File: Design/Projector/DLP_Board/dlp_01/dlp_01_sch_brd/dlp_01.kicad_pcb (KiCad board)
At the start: 6 copper layers, 102 x 98 mm, 238 parts, among them J1 Conn_02x40_Odd_Even, J2 Conn_02x40_Odd_Even, J3 Barrel_Jack_MountingPin, J4 Screw_Terminal_01x03, J5 Screw_Terminal_01x03, J6 Conn_01x03_Male, J7 Conn_01x03_Male, J8 Conn_01x03_Male, J9 Conn_01x03_Male, Q1 2N7000, U1 DLPC3437, U2 DLPC3437, U3 ASDMB-24.000MHZ-LC-T, U4 W25Q64JVSSIQ, U5 W25Q64JVSSIQ, U6 DLPA3000, U7 DLP3310AFQM, U8 RPM5.0-3.0, U9 NF_SN74AUP1T17

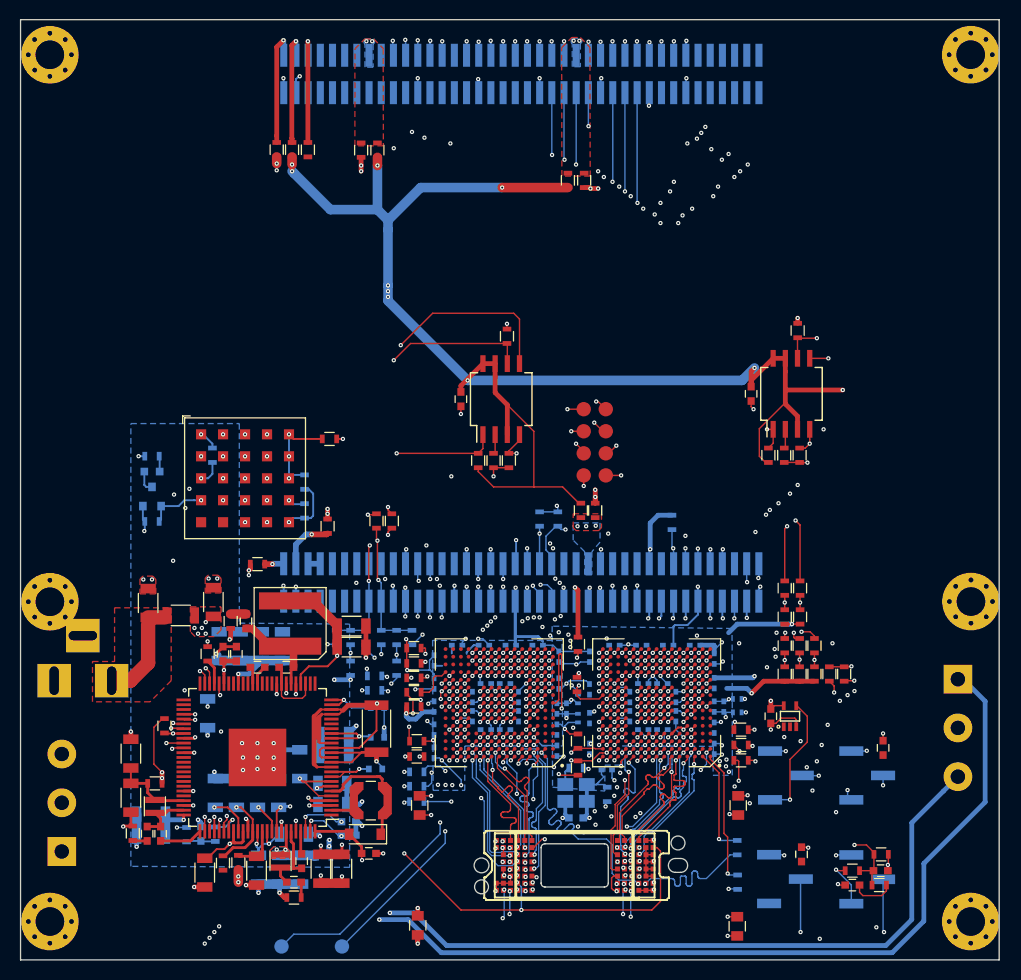
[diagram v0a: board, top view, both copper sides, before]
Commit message: Updated DLP board design
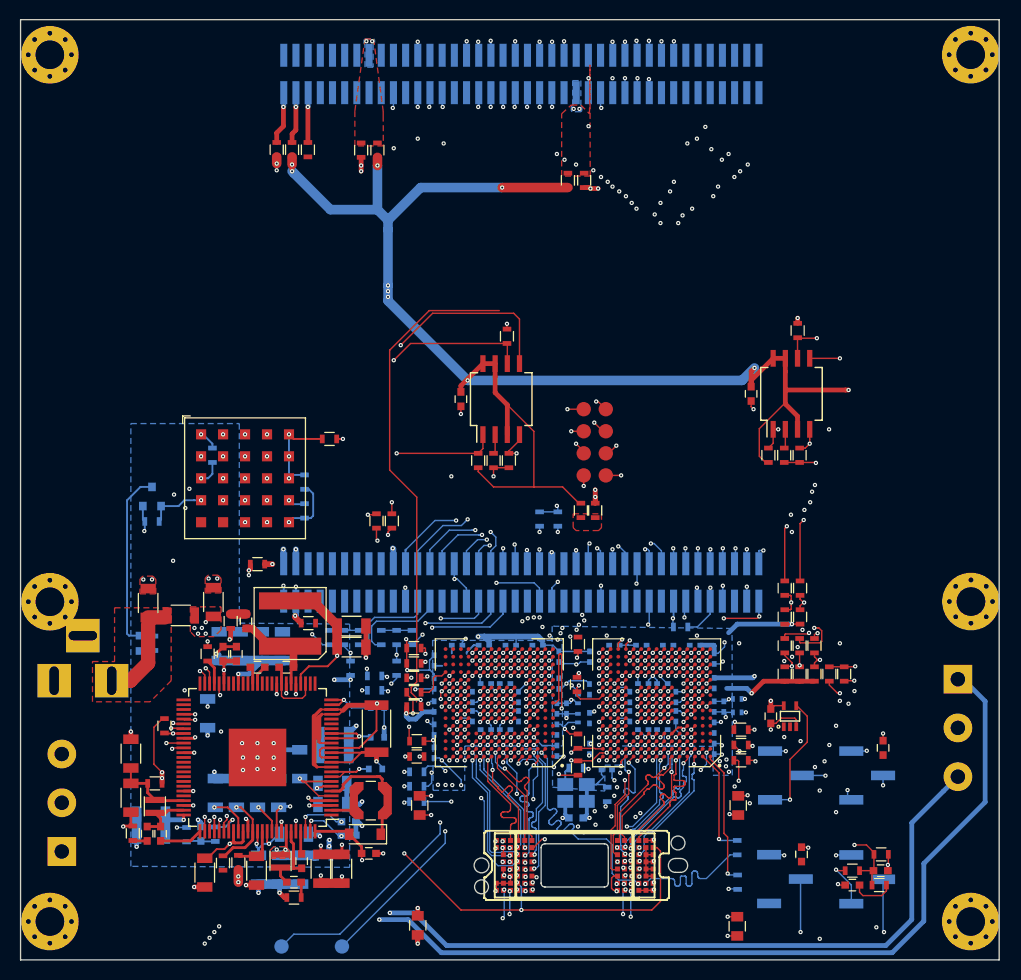
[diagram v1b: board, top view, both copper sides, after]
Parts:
- moved R96 19.5 mm to (110.4, 118.0), turned to 90 degrees
- moved D5 17.9 mm to (108.9, 118.0), turned to 270 degrees
- moved R51 10.9 mm to (165.3, 116.3), turned to 180 degrees
- moved R80 10.3 mm to (126.5, 115.9), turned to 0 degrees
- moved R35 0.70 mm to (130.2, 117.4)
- moved R46 0.70 mm to (128.7, 117.4)
- moved R81 0.70 mm to (131.8, 117.4)
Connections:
- J1 pad 1: Net-(J1-Pad1) -> GND
- J1 pad 10: /application_connectors/JTAG_TDI -> /application_connectors/IO_B13_LN11
- J1 pad 11: /application_connectors/IO_B13_LP12 -> /application_connectors/JTAG_TDO
- J1 pad 12: /application_connectors/JTAG_TDO -> /application_connectors/IO_B13_LP12
- J1 pad 13: /application_connectors/IO_B13_LN12 -> /application_connectors/JTAG_NTRST
- J1 pad 14: /application_connectors/JTAG_NTRST -> /application_connectors/IO_B13_LN12
- J1 pad 15: /application_connectors/ZYNQ_VDDIO_13 -> /application_connectors/IO_B13_LP14
- J1 pad 16: /application_connectors/IO_B13_LP14 -> /application_connectors/ZYNQ_VDDIO_13
- J1 pad 17: /application_connectors/IO_B13_LP13 -> /application_connectors/IO_B13_LN14
- J1 pad 18: /application_connectors/IO_B13_LN14 -> /application_connectors/IO_B13_LP13
- J1 pad 19: /application_connectors/PDM_CVS_TE_B -> /application_connectors/IO_B13_LP21
- J1 pad 2: GND -> Net-(J1-Pad2)
- J1 pad 20: /application_connectors/IO_B13_LP21 -> /application_connectors/PDM_CVS_TE_B
- J1 pad 21: /application_connectors/HSYNC_B -> /application_connectors/IO_B13_LN21
- J1 pad 22: /application_connectors/IO_B13_LN21 -> /application_connectors/HSYNC_B
- J1 pad 23: /application_connectors/VSYNC_B -> GND
- J1 pad 24: GND -> /application_connectors/VSYNC_B
- J1 pad 25: GND -> /application_connectors/IO_B34_LP1
- J1 pad 26: /application_connectors/IO_B34_LP1 -> GND
- J1 pad 27: /application_connectors/DATEN_B -> /application_connectors/IO_B34_LN1
- J1 pad 28: /application_connectors/IO_B34_LN1 -> /application_connectors/DATEN_B
- J1 pad 29: /application_connectors/IO_B34_LN2 -> /application_connectors/IO_B34_LP3
- J1 pad 3: Net-(J1-Pad3) -> GND
- J1 pad 30: /application_connectors/IO_B34_LP3 -> /application_connectors/IO_B34_LN2
- J1 pad 31: /application_connectors/IO_B34_LP4 -> /application_connectors/IO_B34_LN3
- J1 pad 32: /application_connectors/IO_B34_LN3 -> /application_connectors/IO_B34_LP4
- J1 pad 33: /application_connectors/IO_B34_LN4 -> GND
- J1 pad 34: GND -> /application_connectors/IO_B34_LN4
- J1 pad 35: GND -> /application_connectors/IO_B34_LP5
- J1 pad 36: /application_connectors/IO_B34_LP5 -> GND
- J1 pad 37: /application_connectors/IO_B34_LP6 -> /application_connectors/IO_B34_LN5
- J1 pad 38: /application_connectors/IO_B34_LN5 -> /application_connectors/IO_B34_LP6
- J1 pad 39: /application_connectors/IO_B34_LN6 -> /application_connectors/IO_B34_LP7
- J1 pad 4: GND -> Net-(J1-Pad4)
- J1 pad 40: /application_connectors/IO_B34_LP7 -> /application_connectors/IO_B34_LN6
- J1 pad 41: /application_connectors/IO_B34_LP8 -> /application_connectors/IO_B34_LN7
- J1 pad 42: /application_connectors/IO_B34_LN7 -> /application_connectors/IO_B34_LP8
- J1 pad 43: /application_connectors/IO_B34_LN8 -> GND
- J1 pad 44: GND -> /application_connectors/IO_B34_LN8
- J1 pad 45: /application_connectors/IO_B34_LP11 -> /application_connectors/LCD_DATA2
- J1 pad 46: /application_connectors/LCD_DATA2 -> /application_connectors/IO_B34_LP11
- J1 pad 47: /application_connectors/IO_B34_LN11 -> /application_connectors/LCD_DATA3
- J1 pad 48: /application_connectors/LCD_DATA3 -> /application_connectors/IO_B34_LN11
- J1 pad 49: /application_connectors/ZYNQ_VDDIO_34 -> /application_connectors/LCD_DATA6
- J1 pad 5: Net-(J1-Pad5) -> /application_connectors/JTAG_TCK
- J1 pad 50: /application_connectors/LCD_DATA6 -> /application_connectors/ZYNQ_VDDIO_34
- J1 pad 51: /application_connectors/LCD_DATA0 -> /application_connectors/LCD_DATA7
- J1 pad 52: /application_connectors/LCD_DATA7 -> /application_connectors/LCD_DATA0
- J1 pad 53: /application_connectors/LCD_DATA1 -> GND
- J1 pad 54: GND -> /application_connectors/LCD_DATA1
- J1 pad 55: /application_connectors/LCD_DATA4 -> /application_connectors/LCD_DATA10
- J1 pad 56: /application_connectors/LCD_DATA10 -> /application_connectors/LCD_DATA4
- J1 pad 57: /application_connectors/LCD_DATA5 -> /application_connectors/LCD_DATA11
- J1 pad 58: /application_connectors/LCD_DATA11 -> /application_connectors/LCD_DATA5
- J1 pad 59: /application_connectors/LCD_DATA8 -> /application_connectors/LCD_DATA14
- J1 pad 6: /application_connectors/JTAG_TCK -> Net-(J1-Pad6)
- J1 pad 60: /application_connectors/LCD_DATA14 -> /application_connectors/LCD_DATA8
- J1 pad 61: /application_connectors/LCD_DATA9 -> /application_connectors/LCD_DATA15
- J1 pad 62: /application_connectors/LCD_DATA15 -> /application_connectors/LCD_DATA9
- J1 pad 63: /application_connectors/LCD_DATA12 -> /application_connectors/LCD_DE
- J1 pad 64: /application_connectors/LCD_DE -> /application_connectors/LCD_DATA12
- J1 pad 65: /application_connectors/LCD_DATA13 -> /application_connectors/LCD_PCLK
- J1 pad 66: /application_connectors/LCD_PCLK -> /application_connectors/LCD_DATA13
- J1 pad 69: /application_connectors/LCD_HSYNC -> /application_connectors/LCD_VSYNC
- J1 pad 7: /application_connectors/IO_B13_LP11 -> /application_connectors/JTAG_TMS
- J1 pad 70: /application_connectors/LCD_VSYNC -> /application_connectors/LCD_HSYNC
- J1 pad 71: /application_connectors/I2S_SCLK -> /application_connectors/I2S_FSYNC_OUT
- J1 pad 72: /application_connectors/I2S_FSYNC_OUT -> /application_connectors/I2S_SCLK
- J1 pad 73: /application_connectors/I2S_FSYNC_IN -> /application_connectors/I2S_Dout
- J1 pad 74: /application_connectors/I2S_Dout -> /application_connectors/I2S_FSYNC_IN
- J1 pad 75: /application_connectors/I2S_Din -> /application_connectors/I2C0_SDA
- J1 pad 76: /application_connectors/I2C0_SDA -> /application_connectors/I2S_Din
- J1 pad 77: /application_connectors/HDMI_INT -> /application_connectors/I2C0_SCL
- J1 pad 78: /application_connectors/I2C0_SCL -> /application_connectors/HDMI_INT
- J1 pad 79: /application_connectors/MEMS_INTn -> /application_connectors/BP
- J1 pad 8: /application_connectors/JTAG_TMS -> /application_connectors/IO_B13_LP11
- J1 pad 80: /application_connectors/BP -> /application_connectors/MEMS_INTn
- J1 pad 9: /application_connectors/IO_B13_LN11 -> /application_connectors/JTAG_TDI
- J2 pad 1: Net-(J2-Pad1) -> GND
- J2 pad 10: /application_connectors/XADC_GND -> Net-(J2-Pad10)
- J2 pad 11: /application_connectors/PS_MIO0 -> /application_connectors/PS_MIO10
- J2 pad 12: /application_connectors/PS_MIO10 -> /application_connectors/PS_MIO0
- J2 pad 13: /application_connectors/PS_MIO8 -> /application_connectors/PS_MIO11
- J2 pad 14: /application_connectors/PS_MIO11 -> /application_connectors/PS_MIO8
- J2 pad 15: /application_connectors/PS_MIO9 -> /application_connectors/CONTR0_SCL
- J2 pad 16: /application_connectors/CONTR0_SCL -> /application_connectors/PS_MIO9
- J2 pad 17: /application_connectors/PS_MIO12 -> /application_connectors/CONTR0_SDA
- J2 pad 18: /application_connectors/CONTR0_SDA -> /application_connectors/PS_MIO12
- J2 pad 19: /application_connectors/PS_MIO13 -> GND
- J2 pad 2: GND -> Net-(J2-Pad2)
- J2 pad 20: GND -> /application_connectors/PS_MIO13
- J2 pad 21: GND -> /application_connectors/IO_B35_LP2
- J2 pad 22: /application_connectors/IO_B35_LP2 -> GND
- J2 pad 23: /application_connectors/IO_B35_LP1 -> /application_connectors/IO_B35_LN2
- J2 pad 24: /application_connectors/IO_B35_LN2 -> /application_connectors/IO_B35_LP1
- J2 pad 25: /application_connectors/IO_B35_LN1 -> /application_connectors/IO_B35_LP4
- J2 pad 26: /application_connectors/IO_B35_LP4 -> /application_connectors/IO_B35_LN1
- J2 pad 27: /application_connectors/IO_B35_LP3 -> /application_connectors/IO_B35_LN4
- J2 pad 28: /application_connectors/IO_B35_LN4 -> /application_connectors/IO_B35_LP3
- J2 pad 29: /application_connectors/IO_B35_LN3 -> GND
- J2 pad 3: Net-(J2-Pad3) -> GND
- J2 pad 30: GND -> /application_connectors/IO_B35_LN3
- J2 pad 31: GND -> /application_connectors/IO_B35_LP6
- J2 pad 32: /application_connectors/IO_B35_LP6 -> GND
- J2 pad 33: /application_connectors/FPGA_RDY -> /application_connectors/IO_B35_LN6
- J2 pad 34: /application_connectors/IO_B35_LN6 -> /application_connectors/FPGA_RDY
- J2 pad 35: /application_connectors/ACT_SYNC -> /application_connectors/IO_B35_LP8
- J2 pad 36: /application_connectors/IO_B35_LP8 -> /application_connectors/ACT_SYNC
- J2 pad 37: /application_connectors/SUB_FRAME -> /application_connectors/IO_B35_LN8
- J2 pad 38: /application_connectors/IO_B35_LN8 -> /application_connectors/SUB_FRAME
- J2 pad 39: /application_connectors/PROJ_ON -> GND
- J2 pad 4: GND -> Net-(J2-Pad4)
- J2 pad 40: GND -> /application_connectors/PROJ_ON
- J2 pad 41: GND -> /application_connectors/IO_B35_LP10
- J2 pad 42: /application_connectors/IO_B35_LP10 -> GND
- J2 pad 43: /application_connectors/sHOST_IRQ -> /application_connectors/IO_B35_LN10
- J2 pad 44: /application_connectors/IO_B35_LN10 -> /application_connectors/sHOST_IRQ
- J2 pad 45: /application_connectors/mHOST_IRQ -> /application_connectors/PCLK_A
- J2 pad 46: /application_connectors/PCLK_A -> /application_connectors/mHOST_IRQ
- J2 pad 47: /application_connectors/IO_B35_LP11 -> /application_connectors/IO_B35_LN12
- J2 pad 48: /application_connectors/IO_B35_LN12 -> /application_connectors/IO_B35_LP11
- J2 pad 49: /application_connectors/IO_B35_LN11 -> GND
- J2 pad 5: /application_connectors/XADC_INN0 -> /application_connectors/XADC_TEMP_P
- J2 pad 50: GND -> /application_connectors/IO_B35_LN11
- J2 pad 51: /application_connectors/ZYNQ_VDDIO_35 -> /application_connectors/IO_B35_LP14
- J2 pad 52: /application_connectors/IO_B35_LP14 -> /application_connectors/ZYNQ_VDDIO_35
- J2 pad 53: /application_connectors/PCLK_B -> /application_connectors/IO_B35_LN14
- J2 pad 54: /application_connectors/IO_B35_LN14 -> /application_connectors/PCLK_B
- J2 pad 55: /application_connectors/IO_B35_LN13 -> /application_connectors/IO_B35_LP16
- J2 pad 56: /application_connectors/IO_B35_LP16 -> /application_connectors/IO_B35_LN13
- J2 pad 57: /application_connectors/IO_B35_LP15 -> /application_connectors/IO_B35_LN16
- J2 pad 58: /application_connectors/IO_B35_LN16 -> /application_connectors/IO_B35_LP15
- J2 pad 59: /application_connectors/IO_B35_LN15 -> GND
- J2 pad 6: /application_connectors/XADC_TEMP_P -> /application_connectors/XADC_INN0
- J2 pad 60: GND -> /application_connectors/IO_B35_LN15
- J2 pad 61: GND -> /application_connectors/IO_B35_LP18
- J2 pad 62: /application_connectors/IO_B35_LP18 -> GND
- J2 pad 63: /application_connectors/IO_B35_LP17 -> /application_connectors/IO_B35_LN18
- J2 pad 65: /application_connectors/PDM_CVS_TE_A -> /application_connectors/IO_B35_LP20
- J2 pad 66: /application_connectors/IO_B35_LP20 -> /application_connectors/PDM_CVS_TE_A
- J2 pad 67: /application_connectors/HSYNC_A -> /application_connectors/IO_B35_LN20
- J2 pad 68: /application_connectors/IO_B35_LN20 -> /application_connectors/HSYNC_A
- J2 pad 69: /application_connectors/VSYNC_A -> GND
- J2 pad 7: /application_connectors/XADC_INN0 -> /application_connectors/XADC_TEMP_N
- J2 pad 70: GND -> /application_connectors/VSYNC_A
- J2 pad 71: GND -> /application_connectors/IO_B35_LP22
- J2 pad 72: /application_connectors/IO_B35_LP22 -> GND
- J2 pad 73: /application_connectors/DATEN_A -> /application_connectors/IO_B35_LN22
- J2 pad 74: /application_connectors/IO_B35_LN22 -> /application_connectors/DATEN_A
- J2 pad 75: /application_connectors/IO_B35_LN21 -> /application_connectors/IO_B35_LP24
- J2 pad 76: /application_connectors/IO_B35_LP24 -> /application_connectors/IO_B35_LN21
- J2 pad 77: /application_connectors/IO_B35_LP23 -> /application_connectors/IO_B35_LN24
- J2 pad 78: /application_connectors/IO_B35_LN24 -> /application_connectors/IO_B35_LP23
- J2 pad 79: /application_connectors/IO_B35_LN23 -> GND
- J2 pad 8: /application_connectors/XADC_TEMP_N -> /application_connectors/XADC_INN0
- J2 pad 80: GND -> /application_connectors/IO_B35_LN23
- J2 pad 9: Net-(J2-Pad9) -> /application_connectors/XADC_GND
- R70 pad 1: Net-(J1-Pad5) -> Net-(J1-Pad6)
- R71 pad 1: Net-(J1-Pad3) -> Net-(J1-Pad4)
- R77 pad 1: Net-(J1-Pad1) -> Net-(J1-Pad2)
- R80 pad 1: Net-(J2-Pad3) -> Net-(J2-Pad4)
- R89 pad 1: Net-(J2-Pad1) -> Net-(J2-Pad2)
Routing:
- net /application_connectors/LCD_DATA15: track 61.4 -> 120.3 mm
- net /application_connectors/HSYNC_B: track 105.0 -> 47.2 mm, vias 4 -> 1
- net /application_connectors/PROJ_ON: track 87.7 -> 52.4 mm, vias 5 -> 3
- net /application_connectors/PDM_CVS_TE_B: track 125.6 -> 160.1 mm
- net GND: track 323.6 -> 300.5 mm, vias 242 -> 234
- net Net-(D5-Pad1): track 2.28 -> 18.5 mm
- net Net-(J1-Pad1): track 12.5 -> 0.00 mm, vias 1 -> 0
- net Net-(J1-Pad3): track 12.2 -> 0.00 mm, vias 1 -> 0
- net /application_connectors/PDM_CVS_TE_A: track 32.8 -> 20.8 mm
- net Net-(J1-Pad5): track 12.0 -> 0.00 mm, vias 1 -> 0
- net /application_connectors/CONTR0_SCL: track 63.7 -> 52.8 mm, vias 4 -> 2
- net /application_connectors/HSYNC_A: track 34.8 -> 23.9 mm, vias 3 -> 2
- net /application_connectors/IO_B35_LN2: track 12.8 -> 23.3 mm, vias 3 -> 2
- net /application_connectors/IO_B35_LP4: track 13.2 -> 22.6 mm, vias 3 -> 2
- net /application_connectors/IO_B35_LN23: track 39.9 -> 30.6 mm
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- removed copper zone on B.Cu, net /application_connectors/ZYNQ_VDDIO_35

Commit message: Dump of uncommitted changes
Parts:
- added J10: Conn_02x40_Odd_Even, Connector_PinSocket_1.27mm:PinSocket_2x40_P1.27mm_Vertical_SMD, F.Cu at (148.7, 58.7)
- added R100: NF, Resistor_SMD:R_0603_1608Metric, F.Cu at (104.1, 98.4)
- added R101: 0R, Resistor_SMD:R_0603_1608Metric, F.Cu at (104.1, 101.4)
- added R102: 0R, Resistor_SMD:R_0805_2012Metric, B.Cu at (123.5, 125.3)
- added R103: NF, Resistor_SMD:R_0603_1608Metric, F.Cu at (178.1, 67.6)
- added R104: NF, Resistor_SMD:R_0603_1608Metric, F.Cu at (179.5, 67.6)
- added R105: NF, Resistor_SMD:R_0603_1608Metric, B.Cu at (155.2, 69.7)
- added R106: NF, Resistor_SMD:R_0603_1608Metric, B.Cu at (153.5, 69.7)
- added R107: NF, Resistor_SMD:R_0603_1608Metric, B.Cu at (132.0, 66.6)
- added R108: NF, Resistor_SMD:R_0603_1608Metric, B.Cu at (133.7, 66.6)
- added R109: NF, Resistor_SMD:R_0603_1608Metric, F.Cu at (126.4, 66.6)
- added R110: NF, Resistor_SMD:R_0603_1608Metric, F.Cu at (124.8, 66.6)
- added R111: NF, Resistor_SMD:R_0603_1608Metric, F.Cu at (123.2, 66.5)
- added R112: NF, Resistor_SMD:R_0603_1608Metric, F.Cu at (180.9, 67.6)
- added R113: NF, Resistor_SMD:R_0603_1608Metric, F.Cu at (185.5, 67.6)
- added R114: NF, Resistor_SMD:R_0603_1608Metric, F.Cu at (186.8, 67.6)
- added R115: NF, Resistor_SMD:R_0603_1608Metric, F.Cu at (184.2, 67.6)
- added R75: NF, Resistor_SMD:R_0603_1608Metric, F.Cu at (104.1, 91.1)
- added R76: NF, Resistor_SMD:R_0603_1608Metric, F.Cu at (104.1, 89.6)
- added R79: 0R, Resistor_SMD:R_0603_1608Metric, F.Cu at (104.1, 92.5)
- added R83: NF, Resistor_SMD:R_0603_1608Metric, F.Cu at (104.0, 102.9)
- added R84: NF, Resistor_SMD:R_0603_1608Metric, F.Cu at (104.0, 104.3)
- added R85: 0R, Resistor_SMD:R_0603_1608Metric, F.Cu at (104.0, 105.7)
- added R86: NF, Resistor_SMD:R_0603_1608Metric, F.Cu at (104.1, 96.9)
- added R87: NF, Resistor_SMD:R_0603_1608Metric, F.Cu at (104.1, 95.4)
- added R88: 0R, Resistor_SMD:R_0603_1608Metric, F.Cu at (104.1, 94.0)
- added R90: NF, Resistor_SMD:R_0603_1608Metric, F.Cu at (104.1, 99.8)
- added TP11: TestPoint, TestPoint:TestPoint_Pad_D1.5mm, B.Cu at (157.7, 136.5)
- C1, C10, C11, C12, C13, C14, C15, C16, C17, C18, C19, C2, C20, C21, C22, C23, C24, C25, C26, C27, C28, C29, C3, C30, C31, C32, C33, C34, C35, C36, C37, C38, C39, C4, C40, C41, C42, C43, C44, C45, C46, C5, C6, C7, C8, C9: footprint Capacitors_SMD:C_0402 -> Capacitor_SMD:C_0402_1005Metric
- C100, C47, C54, C58, C62, C63, C67, C70, C74, C75, C79, C82, C95, C96, C97, C98, C99, TH1: footprint Capacitors_SMD:C_0603 -> Capacitor_SMD:C_0603_1608Metric
- C48, C49, C50, C51, C52, C53, C55, C56, C57, C59, C60, C61, C64, C65, C66, C71, C72, C73, C76, C77, C80, C81, C83, C84, C85, C86, C87, C88, C93, C94: footprint Capacitors_SMD:C_1206 -> Capacitor_SMD:C_1206_3216Metric
- C68, C69: value 100n -> 470p; footprint Capacitors_SMD:C_0603 -> Capacitor_SMD:C_0603_1608Metric
- C78: value 1.2n -> 10p; footprint Capacitors_SMD:C_0603 -> Capacitor_SMD:C_0603_1608Metric
- C89, C90, C91, C92: footprint Capacitors_SMD:C_0805 -> Capacitor_SMD:C_0805_2012Metric
- D1: footprint Diodes_SMD:D_SOD-123 -> Diode_SMD:D_SOD-123
- D2, D3, D4: footprint Diodes_SMD:D_SOD-523 -> Diode_SMD:D_SOD-523
- D5: footprint LEDs:LED_0603 -> LED_SMD:LED_0603_1608Metric_Pad1.05x0.95mm_HandSolder
- FB1, FB2, FB3, FB4: footprint Inductors_SMD:L_0402 -> Inductor_SMD:L_0402_1005Metric
- H1, H2, H3, H4, H5, H6: footprint Mounting_Holes:MountingHole_3mm_Pad_Via -> MountingHole:MountingHole_3.2mm_M3_Pad_Via
- J1, J2: footprint Pin_Headers:Pin_Header_Straight_2x40_Pitch1.27mm_SMD -> Connector_PinHeader_1.27mm:PinHeader_2x40_P1.27mm_Vertical_SMD
- J3: footprint Connectors:BARREL_JACK -> Connector_BarrelJack:BarrelJack_Horizontal
- J4, J5: footprint Connectors_Terminal_Blocks:TerminalBlock_bornier-3_P5.08mm -> TerminalBlock:TerminalBlock_bornier-3_P5.08mm
- J6, J7, J8, J9: footprint Pin_Headers:Pin_Header_Straight_1x03_Pitch2.54mm_SMD_Pin1Left -> Connector_PinHeader_2.54mm:PinHeader_1x03_P2.54mm_Vertical_SMD_Pin1Left
- L1, L2: footprint Inductors_SMD:L_Taiyo-Yuden_MD-2020 -> Inductor_SMD:L_Taiyo-Yuden_MD-2020
- L3: footprint Coilcraft:L_Coilcraft_LPS4018 -> Inductor_SMD:L_Coilcraft_LPS4018
- Q1: footprint TO_SOT_Packages_SMD:SOT-23 -> Package_TO_SOT_SMD:SOT-23
- R1, R2, R3: value 7.87k -> 30.1; footprint Resistors_SMD:R_0603 -> Resistor_SMD:R_0603_1608Metric
- R10, R11, R12, R13, R14, R15, R16, R17, R18, R19, R20, R21, R22, R23, R24, R25, R26, R27, R28, R29, R30, R31, R32, R33, R34, R37, R38, R39, R4, R40, R41, R42, R43, R44, R45, R48, R49, R5, R50, R51, R52, R53, R54, R55, R56, R57, R58, R59, R6, R60, R61, R62, R63, R65, R66, R67, R68, R69, R7, R72, R73, R8, R80, R89, R9, R92, R93, R94, R95, R96, R97, R98, R99: footprint Resistors_SMD:R_0603 -> Resistor_SMD:R_0603_1608Metric
- R35, R36, R46, R47, R81, R82: footprint Resistors_SMD:R_0603 -> Resistor_SMD:R_0603_1608Metric; moved to F.Cu
- R64: footprint Resistors_SMD:R_2010 -> Resistor_SMD:R_2010_5025Metric
- R70, R71, R74, R77, R78: footprint Resistors_SMD:R_0603 -> Resistor_SMD:R_0603_1608Metric; moved to B.Cu
- R91: footprint Resistors_SMD:R_1206 -> Resistor_SMD:R_1206_3216Metric
- TP1, TP10, TP2, TP3, TP4, TP5, TP6, TP7, TP8, TP9: footprint Measurement_Points:Measurement_Point_Round-SMD-Pad_Small -> TestPoint:TestPoint_Pad_D1.5mm
- U3: footprint Oscillators:Oscillator_SMD_SeikoEpson_SG210-4pin_2.5x2.0mm_HandSoldering -> Oscillator:Oscillator_SMD_SeikoEpson_SG210-4Pin_2.5x2.0mm_HandSoldering
- U4, U5: footprint Housings_SOIC:SO-8_5.3x6.2mm_Pitch1.27mm -> Package_SO:SO-8_5.3x6.2mm_P1.27mm
- U6: footprint HTQFP-100:HTQFP-100_14x14mm_Pitch0.5mm_EP -> Package_QFP:TQFP-100-1EP_14x14mm_P0.5mm_EP5x5mm
- U8: footprint Converter_DCDC:Converter_DCDC_RECOM_RPMx.x-x.0 -> RECOM:Converter_DCDC_RECOM_RPMx.x-x.0
- moved R46 74.6 mm to (186.8, 70.6)
- moved R35 71.5 mm to (184.2, 70.6)
- moved R49 69.7 mm to (135.5, 68.2), turned to 90 degrees
- moved R36 65.1 mm to (180.9, 70.5)
- moved R47 63.1 mm to (179.5, 70.5)
- moved R28 61.1 mm to (185.5, 70.6), turned to 90 degrees
- moved R29 56.5 mm to (178.1, 70.5), turned to 270 degrees
- moved R66 35.6 mm to (186.2, 138.5), turned to 0 degrees
- moved R82 21.4 mm to (113.0, 120.7), turned to 90 degrees
- moved R81 17.8 mm to (114.3, 120.7)
- moved R74 12.4 mm to (156.2, 116.5), turned to 270 degrees
- moved R78 12.1 mm to (158.2, 115.8), turned to 0 degrees
- moved R80 5.02 mm to (126.7, 110.9)
- moved R39 2.34 mm to (133.5, 119.8), turned to 0 degrees
- moved R17 1.72 mm to (175.4, 110.7)
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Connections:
- J2 pad 15: /application_connectors/CONTR0_SCL -> /application_connectors/PS_MIO14
- J2 pad 17: /application_connectors/CONTR0_SDA -> /application_connectors/PS_MIO15
- J2 pad 45: /application_connectors/PCLK_A -> /application_connectors/IO_B35_LP12
- J2 pad 47: /application_connectors/IO_B35_LN12 -> /application_connectors/PCLK_A
- J2 pad 64: /application_connectors/IO_B35_LN18 -> /application_connectors/IO_B35_LP17
- R1 pad 2: /dlp_controller/SPI1_CSZ0 -> /dlp_controller/dlp_controller_gpio/SPI1_CSZ0
- R2 pad 2: /dlp_controller/SPI1_DOUT -> /dlp_controller/dlp_controller_gpio/SPI1_DOUT
- R28 pad 2: /application_connectors/CONTR0_SCL -> /application_connectors/HOST_SCL
- R29 pad 1: /application_connectors/CONTR0_SDA -> /application_connectors/HOST_SDA
- R3 pad 2: /dlp_controller/SPI1_CLK -> /dlp_controller/dlp_controller_gpio/SPI1_CLK
- R35 pad 2: /application_connectors/CONTR0_SCL -> /application_connectors/CONTR1_SCL
- R36 pad 1: /application_connectors/CONTR0_SDA -> /application_connectors/CONTR1_SDA
- R81 pad 1: /application_connectors/IO_B35_LP1 -> /dlp_controller/SPI1_DOUT
- R81 pad 2: /application_connectors/CONTR0_SCL -> GND
- R82 pad 1: /application_connectors/CONTR0_SDA -> /dlp_controller/SPI1_CLK
- R82 pad 2: /application_connectors/IO_B35_LN1 -> GND
- U1 pad C14: /dlp_controller/SPI1_DIN -> /dlp_controller/dlp_controller_gpio/SPI1_DIN
- U3 pad 1: +1V8 -> Net-(TP11-Pad1)
- U6 pad 37: Net-(U6-Pad37) -> GND
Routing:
- net /dlp_controller/dlp_controller_gpio/SPI1_CLK: track 0.00 -> 122.2 mm
- net /dlp_controller/dlp_controller_gpio/SPI1_DOUT: track 0.00 -> 108.7 mm, vias 0 -> 3
- net /dlp_controller/dlp_controller_config/mSPI_MOSI: track 51.3 -> 144.2 mm, vias 3 -> 5
- net Net-(R36-Pad2): track 11.7 -> 103.6 mm, vias 2 -> 4
- net /dlp_controller/dlp_controller_gpio/SPI1_CSZ0: track 0.00 -> 90.9 mm, vias 0 -> 2
- net Net-(R35-Pad1): track 15.8 -> 105.9 mm, vias 2 -> 4
- net Net-(R46-Pad1): track 23.8 -> 108.1 mm, vias 2 -> 4
- net /dlp_controller/dlp_controller_config/mSPI_CSZO: track 49.4 -> 133.0 mm, vias 4 -> 6
- net /dlp_controller/dlp_controller_config/mSPI_CLK: track 56.6 -> 138.5 mm
- net /dlp_controller/dlp_controller_config/mSPI_MISO: track 59.4 -> 141.1 mm, vias 4 -> 6
- net /dlp_controller/dlp_controller_gpio/SPI1_DIN: track 0.00 -> 74.3 mm, vias 0 -> 3
- net Net-(R47-Pad2): track 13.1 -> 83.1 mm, vias 2 -> 4
- net /dlp_controller/SPI1_DOUT: track 107.8 -> 37.8 mm, vias 4 -> 2
- net /dlp_controller/SPI1_CSZ0: track 101.8 -> 32.2 mm, vias 4 -> 2
- net /dlp_controller/dlp_controller_config/sSPI_MOSI: track 64.0 -> 125.9 mm, vias 2 -> 5
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- added copper zone on In4.Cu, net +1V8
- removed copper zone on F.Cu, net /application_connectors/ZYNQ_VDDIO_35
